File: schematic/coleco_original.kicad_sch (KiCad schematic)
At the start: 9 parts, among them J2 Conn_01x02

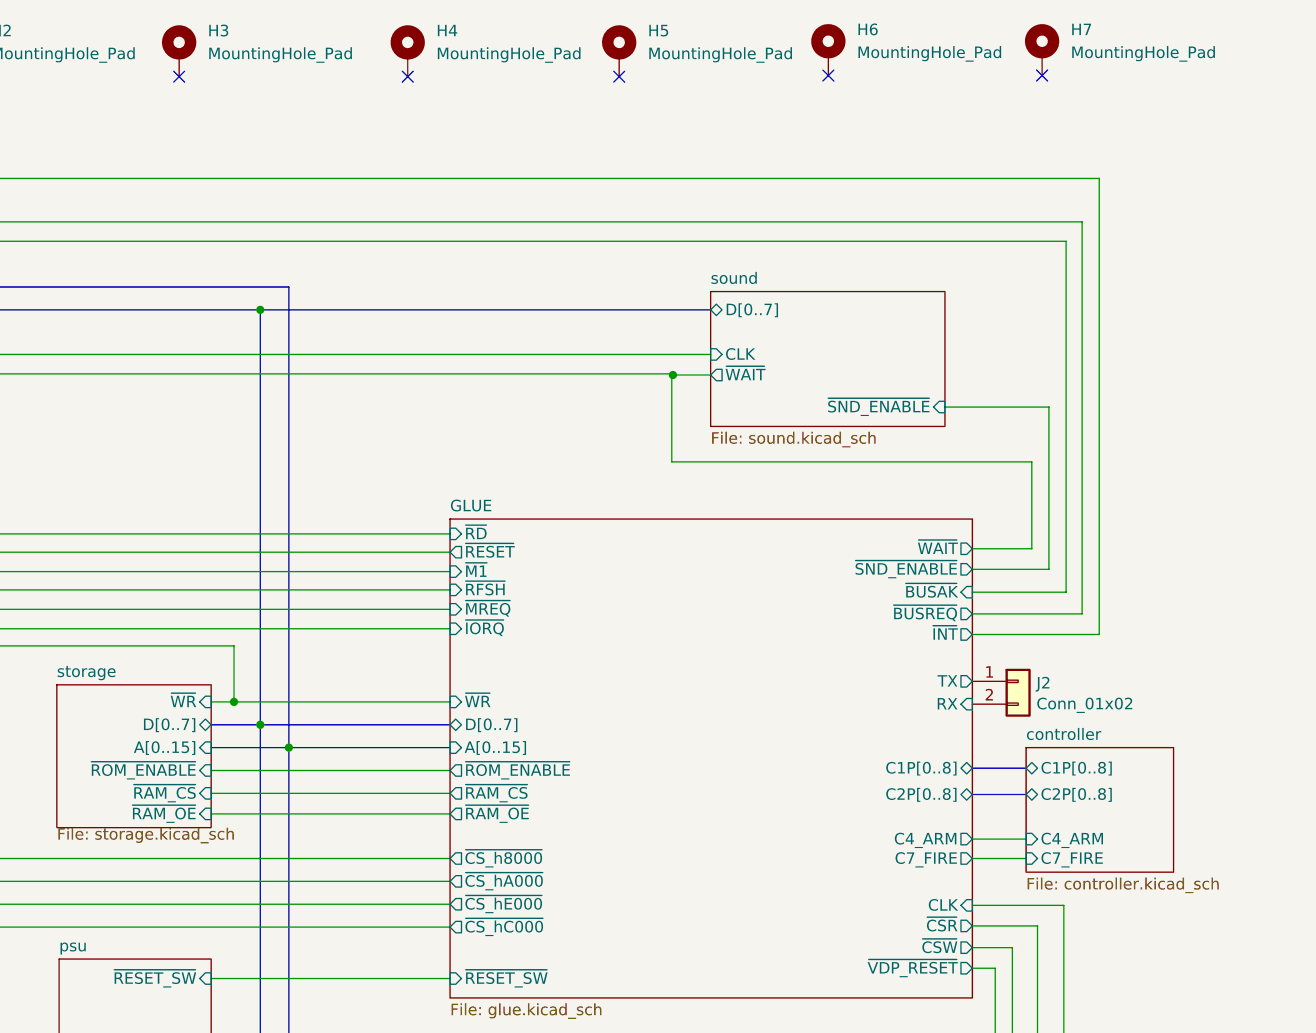
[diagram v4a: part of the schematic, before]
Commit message: first version with roller controller compat
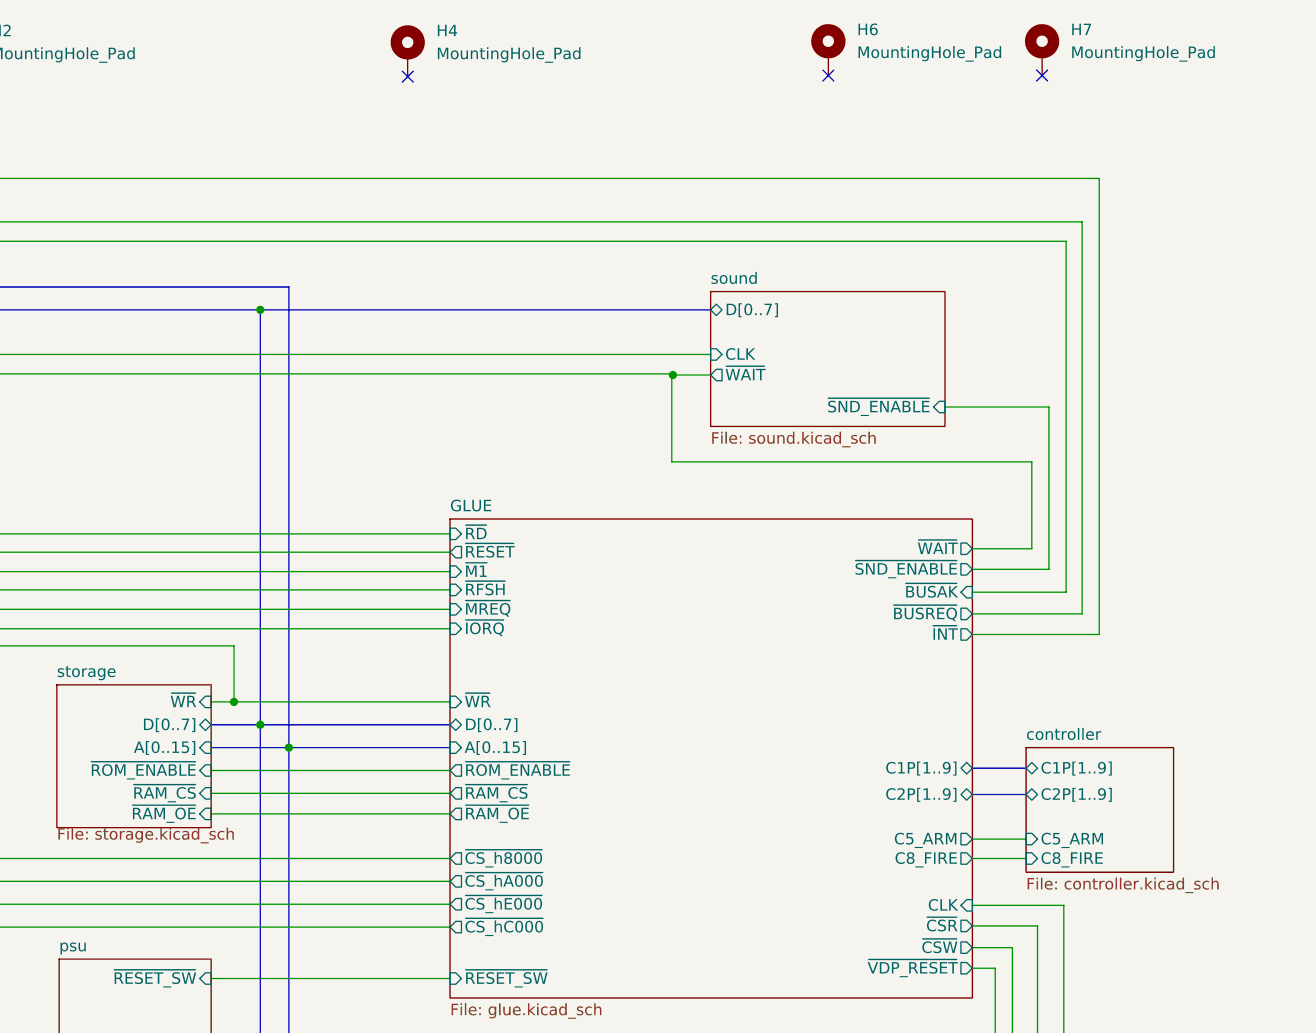
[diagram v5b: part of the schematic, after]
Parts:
- removed H3, H5: MountingHole_Pad, MountingHole:MountingHole_3.2mm_M3_DIN965_Pad, symbol Mechanical:MountingHole_Pad
- removed J2: Conn_01x02, Connector_Molex:Molex_KK-254_AE-6410-02A_1x02_P2.54mm_Vertical, symbol Connector_Generic:Conn_01x02
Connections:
- no-connect marks 8 -> 6
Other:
- sheet GLUE ports: added C1P[1..9], C2P[1..9], C5_ARM, C8_FIRE; removed C1P[0..8], C2P[0..8], C4_ARM, C7_FIRE, RX, TX
- sheet controller ports: added C1P[1..9], C2P[1..9], C5_ARM, C8_FIRE; removed C1P[0..8], C2P[0..8], C4_ARM, C7_FIRE
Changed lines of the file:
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@@
   (no_connect (at 240.157 32.004))
   (no_connect (at 94.742 32.131))
-  (no_connect (at 144.272 32.131))
-  (no_connect (at 193.167 32.131))
   (no_connect (at 169.672 32.131))
   (bus_entry (at 156.464 146.304) (size 2.54 2.54)
@@
   (label "A0" (at 160.782 148.844 0) (fields_autoplaced)
     (effects (font (size 1.27 1.27)) (justify left bottom))
-  )
-  (symbol (lib_id "Mechanical:MountingHole_Pad") (at 193.167 29.591 0) (unit 1)
-    (in_bom yes) (on_board yes) (dnp no) (fields_autoplaced)
-    (property "Reference" "H5" (at 196.342 27.0509 0)
-      (effects (font (size 1.27 1.27)) (justify left))
-    )
-    (property "Value" "MountingHole_Pad" (at 196.342 29.5909 0)
-      (effects (font (size 1.27 1.27)) (justify left))
-    )
-    (property "Footprint" "MountingHole:MountingHole_3.2mm_M3_DIN965_Pad" (at 193.167 29.591 0)
-      (effects (font (size 1.27 1.27)) hide)
-    )
-    (property "Datasheet" "~" (at 193.167 29.591 0)
-      (effects (font (size 1.27 1.27)) hide)
-    )
-    (pin "1")
-    (instances
-      (project "coleco_original"
-        (path "/970e0f64-111f-41e3-9f5a-fb0d0f6fa101"
-          (reference "H5") (unit 1)
-        )
-      )
-    )
   )
   (symbol (lib_id "Mechanical:MountingHole_Pad") (at 120.142 29.591 0) (unit 1)
@@
         (path "/970e0f64-111f-41e3-9f5a-fb0d0f6fa101"
           (reference "H1") (unit 1)
-        )
-      )
-    )
-  )
-  (symbol (lib_id "Mechanical:MountingHole_Pad") (at 144.272 29.591 0) (unit 1)
-    (in_bom yes) (on_board yes) (dnp no) (fields_autoplaced)
-    (property "Reference" "H3" (at 147.447 27.0509 0)
-      (effects (font (size 1.27 1.27)) (justify left))
-    )
-    (property "Value" "MountingHole_Pad" (at 147.447 29.5909 0)
-      (effects (font (size 1.27 1.27)) (justify left))
-    )
-    (property "Footprint" "MountingHole:MountingHole_3.2mm_M3_DIN965_Pad" (at 144.272 29.591 0)
-      (effects (font (size 1.27 1.27)) hide)
-    )
-    (property "Datasheet" "~" (at 144.272 29.591 0)
-      (effects (font (size 1.27 1.27)) hide)
-    )
-    (pin "1")
-    (instances
-      (project "coleco_original"
-        (path "/970e0f64-111f-41e3-9f5a-fb0d0f6fa101"
-          (reference "H3") (unit 1)
-        )
-      )
-    )
-  )
-  (symbol (lib_id "Connector_Generic:Conn_01x02") (at 237.49 99.314 0) (unit 1)
-    (in_bom yes) (on_board yes) (dnp no)
-    (property "Reference" "J2" (at 239.522 99.5172 0)
-      (effects (font (size 1.27 1.27)) (justify left))
-    )
-    (property "Value" "Conn_01x02" (at 239.522 101.8286 0)
-      (effects (font (size 1.27 1.27)) (justify left))
-    )
-    (property "Footprint" "Connector_Molex:Molex_KK-254_AE-6410-02A_1x02_P2.54mm_Vertical" (at 237.49 99.314 0)
-      (effects (font (size 1.27 1.27)) hide)
-    )
-    (property "Datasheet" "~" (at 237.49 99.314 0)
-      (effects (font (size 1.27 1.27)) hide)
-    )
-    (pin "1")
-    (pin "2")
-    (instances
-      (project "coleco_original"
-        (path "/970e0f64-111f-41e3-9f5a-fb0d0f6fa101/00000000-0000-0000-0000-000062624749"
-          (reference "J2") (unit 1)
-        )
-        (path "/970e0f64-111f-41e3-9f5a-fb0d0f6fa101"
-          (reference "J9") (unit 1)
-        )
-      )
-      (project "picerino_sn76489AN"
-        (path "/b5352a33-563a-4ffe-a231-2e68fb54afa3"
-          (reference "J2") (unit 1)
         )
       )
@@
       (effects (font (size 1.27 1.27)) (justify left))
     )
-    (pin "C1P[0..8]" bidirectional (at 232.41 108.966 0)
-      (effects (font (size 1.27 1.27)) (justify right))
-    )
-    (pin "C2P[0..8]" bidirectional (at 232.41 111.887 0)
-      (effects (font (size 1.27 1.27)) (justify right))
-    )
     (pin "~{INT}" output (at 232.41 94.107 0)
       (effects (font (size 1.27 1.27)) (justify right))
@@
       (effects (font (size 1.27 1.27)) (justify left))
     )
-    (pin "RX" input (at 232.41 101.854 0)
-      (effects (font (size 1.27 1.27)) (justify right))
-    )
-    (pin "TX" output (at 232.41 99.314 0)
-      (effects (font (size 1.27 1.27)) (justify right))
-    )
-    (pin "C4_ARM" output (at 232.41 116.84 0)
-      (effects (font (size 1.27 1.27)) (justify right))
-    )
-    (pin "C7_FIRE" output (at 232.41 118.999 0)
-      (effects (font (size 1.27 1.27)) (justify right))
-    )
     (pin "~{BUSREQ}" output (at 232.41 91.821 0)
       (effects (font (size 1.27 1.27)) (justify right))
     )
     (pin "~{BUSAK}" input (at 232.41 89.408 0)
+      (effects (font (size 1.27 1.27)) (justify right))
+    )
+    (pin "C8_FIRE" output (at 232.41 118.999 0)
+      (effects (font (size 1.27 1.27)) (justify right))
+    )
+    (pin "C5_ARM" output (at 232.41 116.84 0)
+      (effects (font (size 1.27 1.27)) (justify right))
+    )
+    (pin "C1P[1..9]" bidirectional (at 232.41 108.966 0)
+      (effects (font (size 1.27 1.27)) (justify right))
+    )
+    (pin "C2P[1..9]" bidirectional (at 232.41 111.887 0)
       (effects (font (size 1.27 1.27)) (justify right))
     )
@@
       (effects (font (size 1.27 1.27)) (justify left top))
     )
-    (pin "C1P[0..8]" bidirectional (at 238.379 108.966 180)
-      (effects (font (size 1.27 1.27)) (justify left))
-    )
-    (pin "C2P[0..8]" bidirectional (at 238.379 111.887 180)
-      (effects (font (size 1.27 1.27)) (justify left))
-    )
-    (pin "C4_ARM" input (at 238.379 116.84 180)
-      (effects (font (size 1.27 1.27)) (justify left))
-    )
-    (pin "C7_FIRE" input (at 238.379 118.999 180)
-      (effects (font (size 1.27 1.27)) (justify left))
-    )
+    (pin "C2P[1..9]" bidirectional (at 238.379 111.887 180)
+      (effects (font (size 1.27 1.27)) (justify left))
+    )
+    (pin "C8_FIRE" input (at 238.379 118.999 180)
+      (effects (font (size 1.27 1.27)) (justify left))
+    )
+    (pin "C5_ARM" input (at 238.379 116.84 180)
+      (effects (font (size 1.27 1.27)) (justify left))
+    )
+    (pin "C1P[1..9]" bidirectional (at 238.379 108.966 180)
+      (effects (font (size 1.27 1.27)) (justify left))
+    )

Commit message: update pdf schematic and schematic wording
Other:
- title: Righteous Tentacle, Colecovision Reverse Engineering Project -> Mini Colecovision
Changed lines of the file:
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@@
   (paper "USLetter")
   (title_block
-    (title "Righteous Tentacle, Colecovision Reverse Engineering Project")
-    (date "2023-06-18")
-    (rev "1.0.0.F")
+    (title "Mini Colecovision")
+    (date "2024-03-25")
+    (rev "1.0.0")
     (company "sparkletron")
     (comment 1 "Jay Convertino")
     (comment 2 "MIT LICENSE")
-    (comment 3 "PCB: 75743 REV F")
+    (comment 3 "TARGET: Portable")
   )
   (junction (at 199.136 65.278) (diameter 0) (color 0 0 0 0)
